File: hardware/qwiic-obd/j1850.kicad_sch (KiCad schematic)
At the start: 41 parts, among them J601 PIC-ICSPPOLAR_LOCK, Q601 DMG2301L, Q602 2N7002, Q603 2N7002, Q604 2N7002, Q605 2N7002, Q606 2N7002, Q607 2N7002, Q608 2N7002, U601 LM317L_SOT-89, U602 NCS20072, U603 PIC16F15225-I{slash}ST

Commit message: Added initial layout (parts dump)
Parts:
- C602: footprint (none) -> Capacitor_SMD:C_0805_2012Metric_Pad1.18x1.45mm_HandSolder
- D601: value BAT46W -> BAT46J
- D604: value BAT54W -> BAT54J; footprint Package_TO_SOT_SMD:SOT-323_SC-70 -> Diode_SMD:D_SOD-123; symbol Diode:BAT54W -> Diode:BAT54J
- U603: footprint TSSOP14_ST_MCH -> UltraLibrarian:PIC16F15225-I&slash_ST
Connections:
- net GND: now also D604.2 (A); no longer D604.1 (A)
- net at R614.1, U602.3 (+): now also D604.1 (K); no longer D604.3 (K)
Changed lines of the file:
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@@
     (pin "2")
   )
-  (symbol (lib_id "Diode:BAT54W") (at 81.28 110.49 270) (unit 1)
+  (symbol (lib_id "Diode:BAT54J") (at 81.28 110.49 270) (unit 1)
     (in_bom yes) (on_board yes)
     (property "Reference" "D604" (id 0) (at 84.5566 109.3216 90)
       (effects (font (size 1.27 1.27)) (justify left))
     )
-    (property "Value" "BAT54W" (id 1) (at 84.5566 111.633 90)
-      (effects (font (size 1.27 1.27)) (justify left))
-    )
-    (property "Footprint" "Package_TO_SOT_SMD:SOT-323_SC-70" (id 2) (at 76.835 110.49 0)
+    (property "Value" "BAT54J" (id 1) (at 84.5566 111.633 90)
+      (effects (font (size 1.27 1.27)) (justify left))
+    )
+    (property "Footprint" "Diode_SMD:D_SOD-123" (id 2) (at 76.835 110.49 0)
       (effects (font (size 1.27 1.27)) hide)
     )
@@
     (pin "1")
     (pin "2")
-    (pin "3")
   )
   (symbol (lib_id "power:GND") (at 255.27 97.79 0) (unit 1)
@@
       (effects (font (size 1.27 1.27)) (justify left))
     )
-    (property "Footprint" "" (id 2) (at 187.6552 44.45 0)
+    (property "Footprint" "Capacitor_SMD:C_0805_2012Metric_Pad1.18x1.45mm_HandSolder" (id 2) (at 187.6552 44.45 0)
       (effects (font (size 1.27 1.27)) hide)
     )
@@
       (effects (font (size 1.524 1.524)))
     )
-    (property "Footprint" "TSSOP14_ST_MCH" (id 2) (at 193.04 127.254 0)
+    (property "Footprint" "UltraLibrarian:PIC16F15225-I&slash_ST" (id 2) (at 193.04 127.254 0)
       (effects (font (size 1.524 1.524)) hide)
     )
@@
     (in_bom yes) (on_board yes)
     (property "Reference" "D601" (id 0) (at 241.3 27.5082 0))
-    (property "Value" "BAT46W" (id 1) (at 241.3 29.8196 0))
+    (property "Value" "BAT46J" (id 1) (at 241.3 29.8196 0))
     (property "Footprint" "Diode_SMD:D_SOD-123" (id 2) (at 241.3 28.575 0)
       (effects (font (size 1.27 1.27)) hide)

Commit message: OK, layout v1 complete
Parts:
- removed R617: 10k, Resistor_SMD:R_0805_2012Metric_Pad1.20x1.40mm_HandSolder, symbol Device:R
- added Q607: 2N7002, Package_TO_SOT_SMD:SOT-23, symbol Transistor_FET:2N7002
- added R609: 10k, Resistor_SMD:R_0805_2012Metric_Pad1.20x1.40mm_HandSolder, symbol Device:R
- renumbered Q607 to Q608, Q608 to Q609, R609 to R610, R610 to R611, R611 to R612, R612 to R613, R613 to R614, R614 to R615, R615 to R616, R616 to R617
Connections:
- net +5V_SW is gone; now on net +5V: R614.1
- net +3V3: now also R609.1
- net GND: now also Q607.2 (S)
- net SAE_PWM: now also Q607.1 (G)
- net SAE_VPW: now also Q607.3 (D), R609.2
- net VBAT renamed +12V

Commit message: Fix title block
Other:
- title: Vehicle CAN Collector -> QWIIC OBDII Interface
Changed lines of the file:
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@@
   (paper "A4")
   (title_block
-    (title "Vehicle CAN Collector")
-    (date "2022-12-29")
+    (title "QWIIC OBDII Interface")
+    (date "2023-01-03")
     (rev "1")
     (company "Gavin Hurlbut")

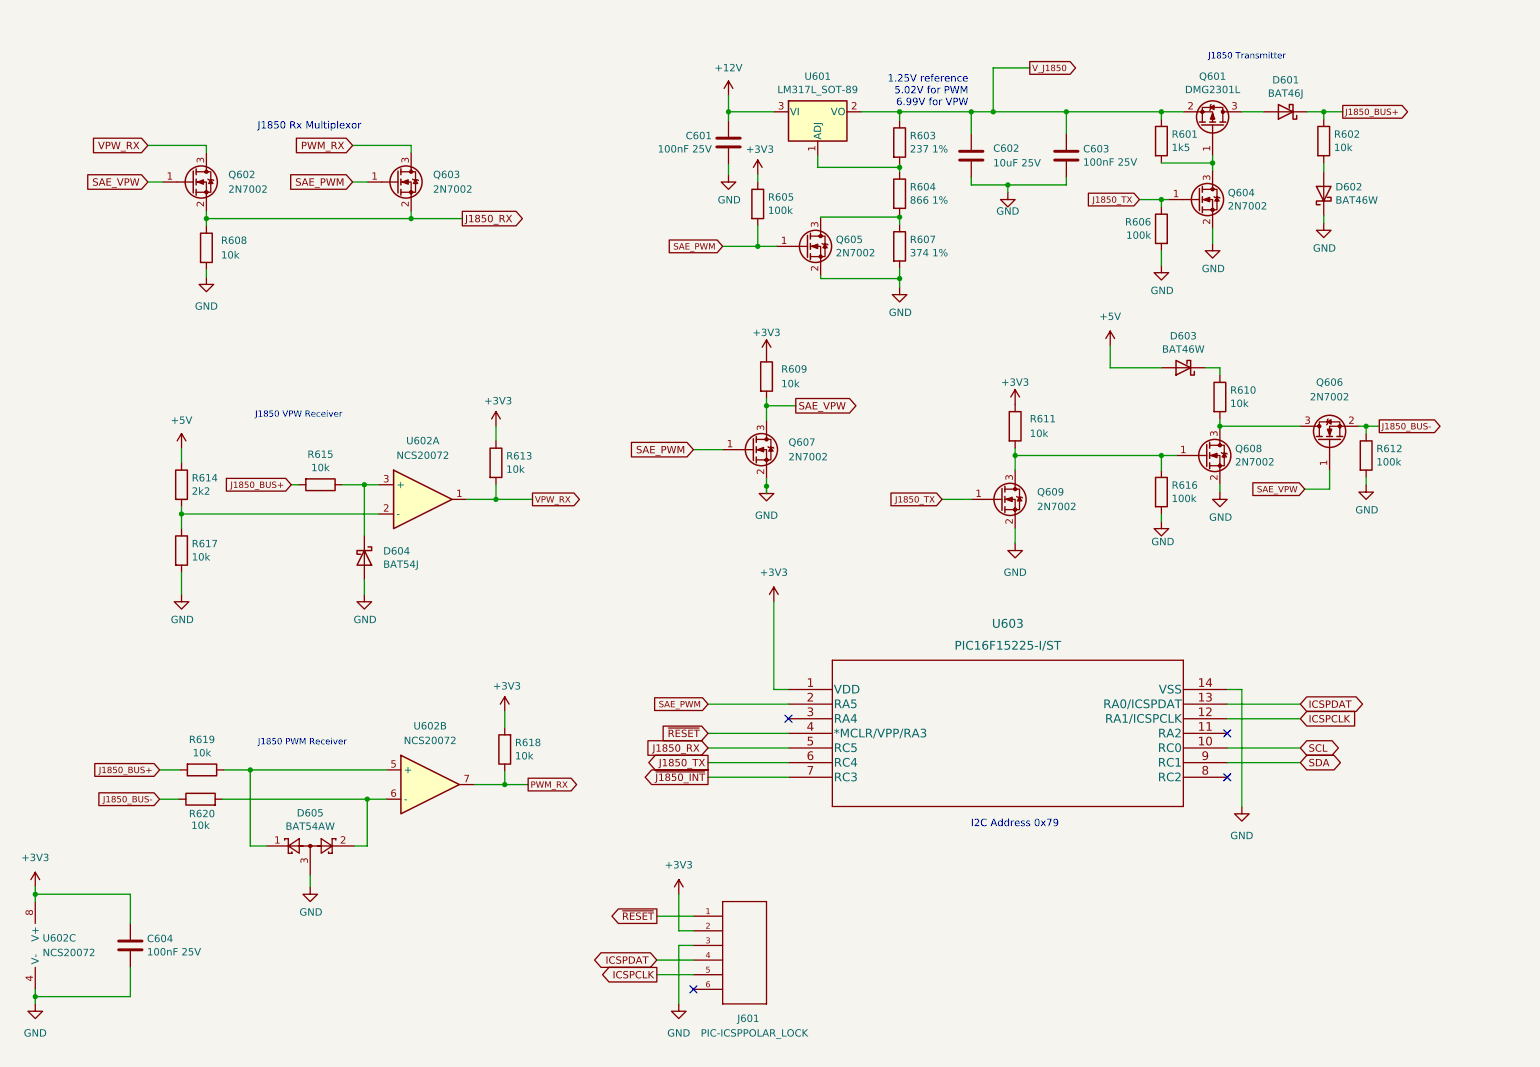
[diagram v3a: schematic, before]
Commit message: Add PIC bootloader, update silkscreen
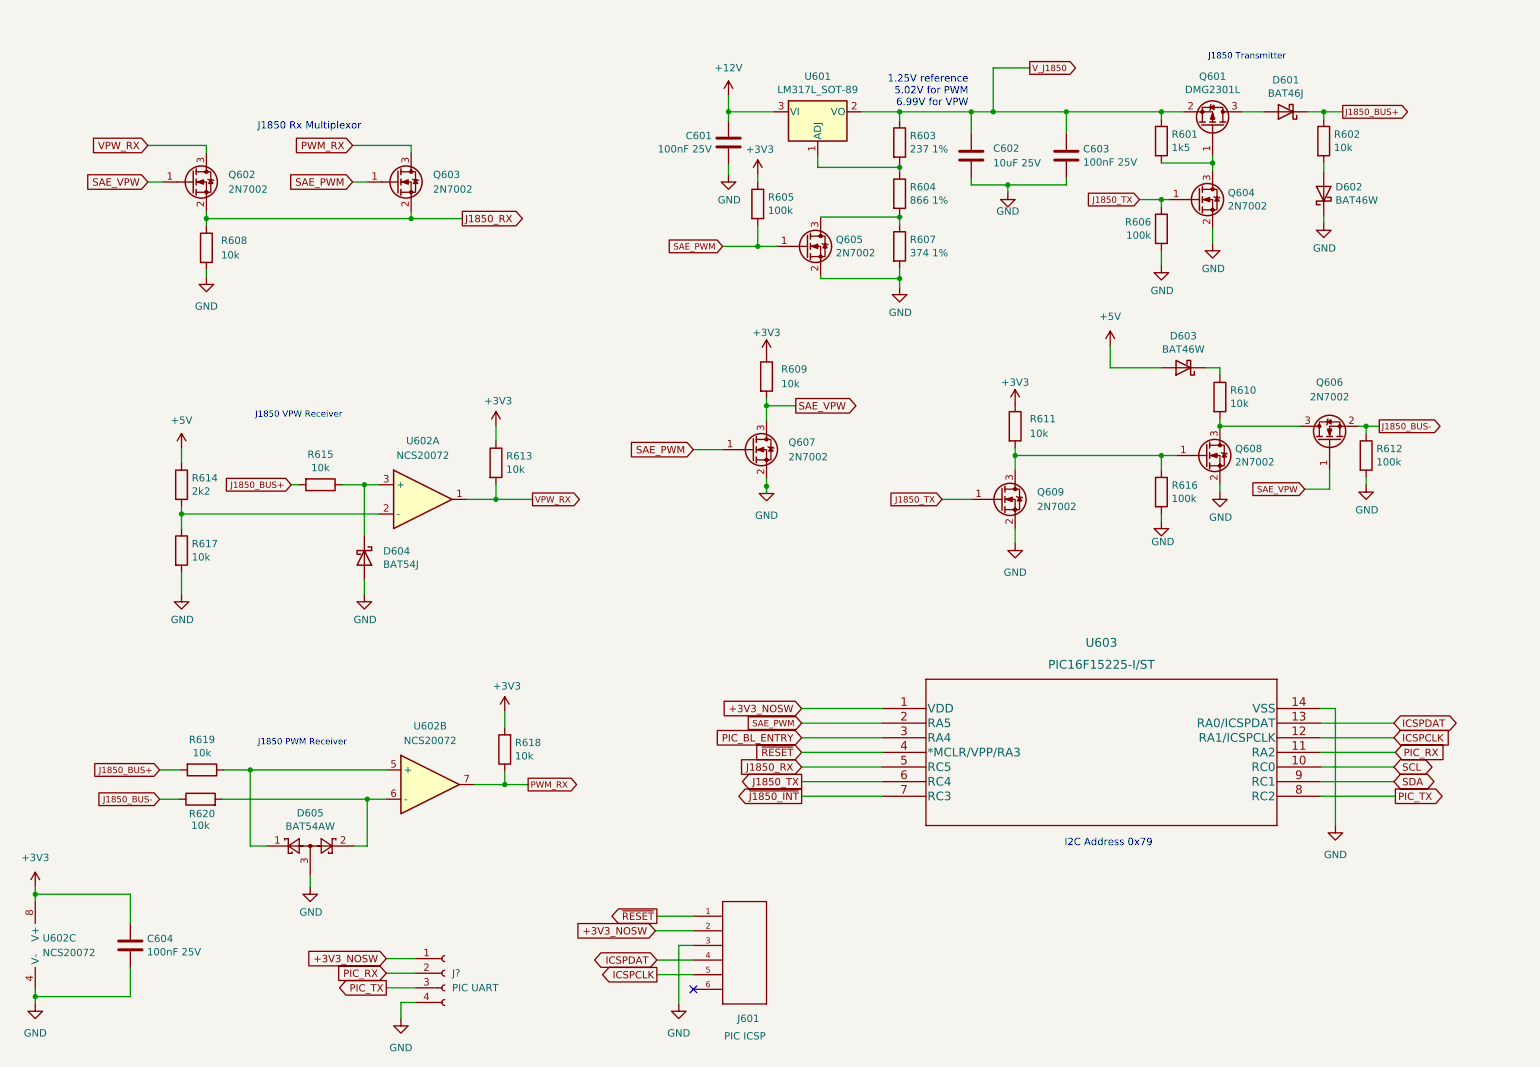
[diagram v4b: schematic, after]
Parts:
- added J?: PIC UART, Connector_PinHeader_2.54mm:PinHeader_1x04_P2.54mm_Vertical, symbol Connector:Conn_01x04_Female
- J601: value PIC-ICSPPOLAR_LOCK -> PIC ICSP
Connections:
- net +3V3: no longer J601.2 (PGC), U603.1 (VDD)
- net GND: now also J?.4 (Pin_4)
- net PIC_RX: now reaches U603.11 (RA2)
- net PIC_RX: now also J?.2 (Pin_2)
- net PIC_BL_ENTRY: now reaches U603.3 (RA4)
- net PIC_TX: now reaches U603.8 (RC2)
- net PIC_TX: now also J?.3 (Pin_3)
- new net +3V3_NOSW: J601.2 (PGC), J?.1 (Pin_1), U603.1 (VDD)
- no-connect marks 4 -> 1
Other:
- moved on the sheet: U603

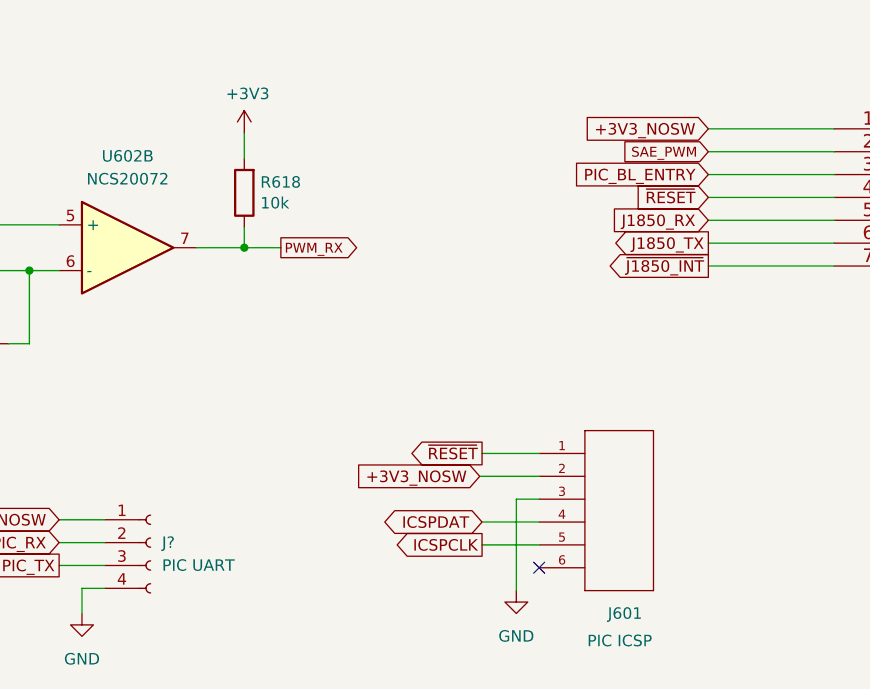
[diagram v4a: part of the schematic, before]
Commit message: Split firmware into two separate projects
- got it building into different parts of the FLASH.
- bootloader - 0x000 - 0x3FF (word addresses)
- application - 0x400 - end  (word addresses)
- reset vector and interrupt vector are also mirrored
  into 0x400 and 0x404 (respectively) for application
  use, and are linked to from the bootloader
- when the BL_ENABLE button is pushed while in the
  application, a falling edge interrupt causes a reset
  back into the bootloader.
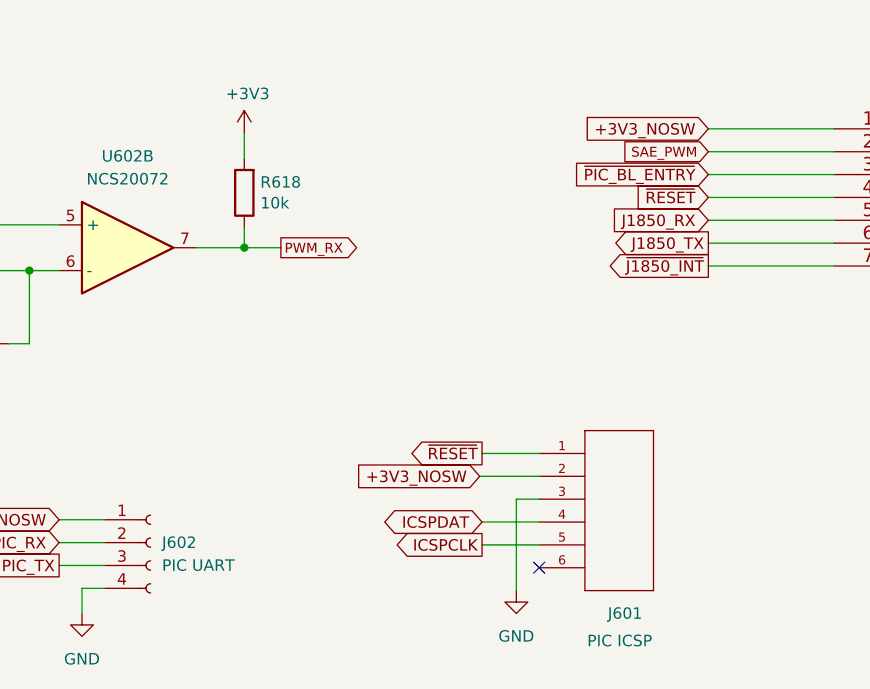
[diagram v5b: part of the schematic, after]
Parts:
- gave numbers to parts that had none: 1
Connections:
- net PIC_BL_ENTRY renamed ~{PIC_BL_ENTRY}
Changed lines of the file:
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@@
     )
   )
-  (global_label "PIC_BL_ENTRY" (shape input) (at 157.226 141.732 180) (fields_autoplaced)
+  (global_label "~{PIC_BL_ENTRY}" (shape input) (at 157.226 141.732 180) (fields_autoplaced)
     (effects (font (size 1.27 1.27)) (justify right))
     (property "Intersheet References" "${INTERSHEET_REFS}" (id 0) (at 141.6291 141.6526 0)
@@
   (symbol (lib_id "power:GND") (at 255.27 97.79 0) (unit 1)
     (in_bom yes) (on_board yes)
-    (property "Reference" "#PWR0614" (id 0) (at 255.27 104.14 0)
+    (property "Reference" "#PWR0615" (id 0) (at 255.27 104.14 0)
       (effects (font (size 1.27 1.27)) hide)
     )
@@
   (symbol (lib_id "power:GND") (at 135.89 187.96 0) (unit 1)
     (in_bom yes) (on_board yes) (fields_autoplaced)
-    (property "Reference" "#PWR0628" (id 0) (at 135.89 194.31 0)
+    (property "Reference" "#PWR0627" (id 0) (at 135.89 194.31 0)
       (effects (font (size 1.27 1.27)) hide)
     )
@@
   (symbol (lib_id "power:GND") (at 151.13 98.044 0) (unit 1)
     (in_bom yes) (on_board yes) (fields_autoplaced)
-    (property "Reference" "#PWR0615" (id 0) (at 151.13 104.394 0)
+    (property "Reference" "#PWR0616" (id 0) (at 151.13 104.394 0)
       (effects (font (size 1.27 1.27)) hide)
     )
@@
   (symbol (lib_id "power:GND") (at 219.71 104.14 0) (unit 1)
     (in_bom yes) (on_board yes)
-    (property "Reference" "#PWR0617" (id 0) (at 219.71 110.49 0)
+    (property "Reference" "#PWR0618" (id 0) (at 219.71 110.49 0)
       (effects (font (size 1.27 1.27)) hide)
     )
@@
   (symbol (lib_id "power:GND") (at 49.53 116.84 0) (unit 1)
     (in_bom yes) (on_board yes)
-    (property "Reference" "#PWR0619" (id 0) (at 49.53 123.19 0)
+    (property "Reference" "#PWR0620" (id 0) (at 49.53 123.19 0)
       (effects (font (size 1.27 1.27)) hide)
     )
@@
   (symbol (lib_id "Connector:Conn_01x04_Female") (at 95.25 182.626 0) (unit 1)
     (in_bom yes) (on_board yes) (fields_autoplaced)
-    (property "Reference" "J?" (id 0) (at 96.52 182.6259 0)
+    (property "Reference" "J602" (id 0) (at 96.52 182.6259 0)
       (effects (font (size 1.27 1.27)) (justify left))
     )
@@
   (symbol (lib_id "power:GND") (at 229.87 99.06 0) (unit 1)
     (in_bom yes) (on_board yes)
-    (property "Reference" "#PWR0616" (id 0) (at 229.87 105.41 0)
+    (property "Reference" "#PWR0617" (id 0) (at 229.87 105.41 0)
       (effects (font (size 1.27 1.27)) hide)
     )
@@
   (symbol (lib_id "power:GND") (at 87.63 190.5 0) (unit 1)
     (in_bom yes) (on_board yes) (fields_autoplaced)
-    (property "Reference" "#PWR?" (id 0) (at 87.63 196.85 0)
+    (property "Reference" "#PWR0628" (id 0) (at 87.63 196.85 0)
       (effects (font (size 1.27 1.27)) hide)
     )
@@
   (symbol (lib_id "power:GND") (at 194.31 107.95 0) (unit 1)
     (in_bom yes) (on_board yes) (fields_autoplaced)
-    (property "Reference" "#PWR0618" (id 0) (at 194.31 114.3 0)
+    (property "Reference" "#PWR0619" (id 0) (at 194.31 114.3 0)
       (effects (font (size 1.27 1.27)) hide)
     )
@@
   (symbol (lib_id "power:GND") (at 81.28 116.84 0) (unit 1)
     (in_bom yes) (on_board yes)
-    (property "Reference" "#PWR0620" (id 0) (at 81.28 123.19 0)
+    (property "Reference" "#PWR0621" (id 0) (at 81.28 123.19 0)
       (effects (font (size 1.27 1.27)) hide)
     )
@@
   (symbol (lib_id "power:GND") (at 24.13 187.96 0) (unit 1)
     (in_bom yes) (on_board yes) (fields_autoplaced)
-    (property "Reference" "#PWR0627" (id 0) (at 24.13 194.31 0)
+    (property "Reference" "#PWR0626" (id 0) (at 24.13 194.31 0)
       (effects (font (size 1.27 1.27)) hide)
     )
@@
   (symbol (lib_id "power:+5V") (at 49.53 91.44 0) (unit 1)
     (in_bom yes) (on_board yes) (fields_autoplaced)
-    (property "Reference" "#PWR0106" (id 0) (at 49.53 95.25 0)
-      (effects (font (size 1.27 1.27)) hide)
-    )
+    (property "Reference" "#PWR0614" (id 0) (at 49.53 95.25 0)
+      (effects (font (size 1.27 1.27)) hide)
+    )
